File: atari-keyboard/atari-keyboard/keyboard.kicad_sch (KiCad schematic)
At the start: 210 parts, among them SW201 MENU, SW202 TURBO, SW203 RESET, SW204 OPTION, SW205 SELECT, SW206 START, SW207 HELP, SW208 ESC, SW209 RSHIFT, SW210 1, SW211 2, SW212 3, SW213 4, SW214 5, SW215 6, SW216 7, SW217 8, SW218 C_UP, SW219 9, SW220 0, SW221 LT, SW222 GT, SW223 BS, SW224 BRK, SW225 TAB, SW226 Q, SW227 C_DOWN, SW228 W, SW229 E, SW230 R, SW231 T, SW232 Y, SW233 U, SW234 I, SW235 O, SW236 C_LEFT, SW237 P, SW238 DASH, SW239 EQUAL, SW240 RET, SW241 CTRL, SW242 A, SW243 S, SW244 D, SW245 C_RIGHT, SW246 F, SW247 G, SW248 H, SW249 J, SW250 K, SW251 L, SW252 SEMI, SW253 PLUS, SW254 N, SW255 ASTRIX, SW256 CAPS, SW257 LSHIFT, SW258 Z, SW259 X, SW260 C, SW261 V, SW262 B, SW263 M, SW264 FN, SW265 INV, SW266 SPACE, SW267 COMMA, SW268 PERIOD, SW269 SLASH, SW270 POWER

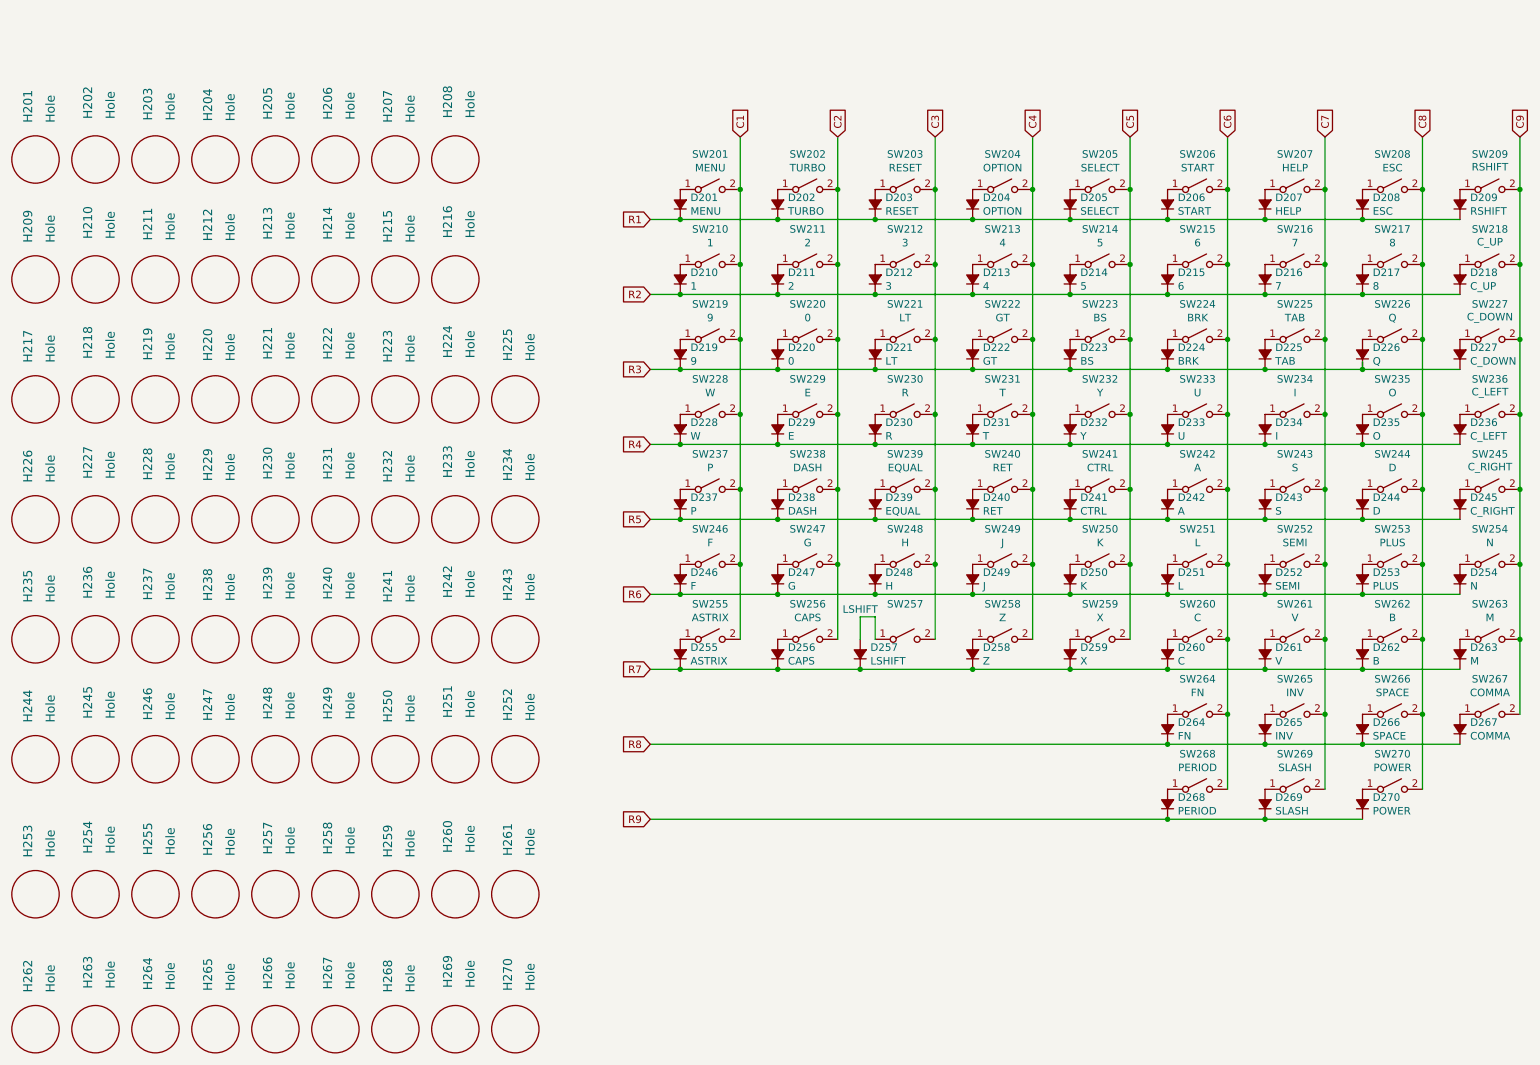
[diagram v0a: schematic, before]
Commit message: Reworked keyboard matrix to be a MUCH cleaner routing
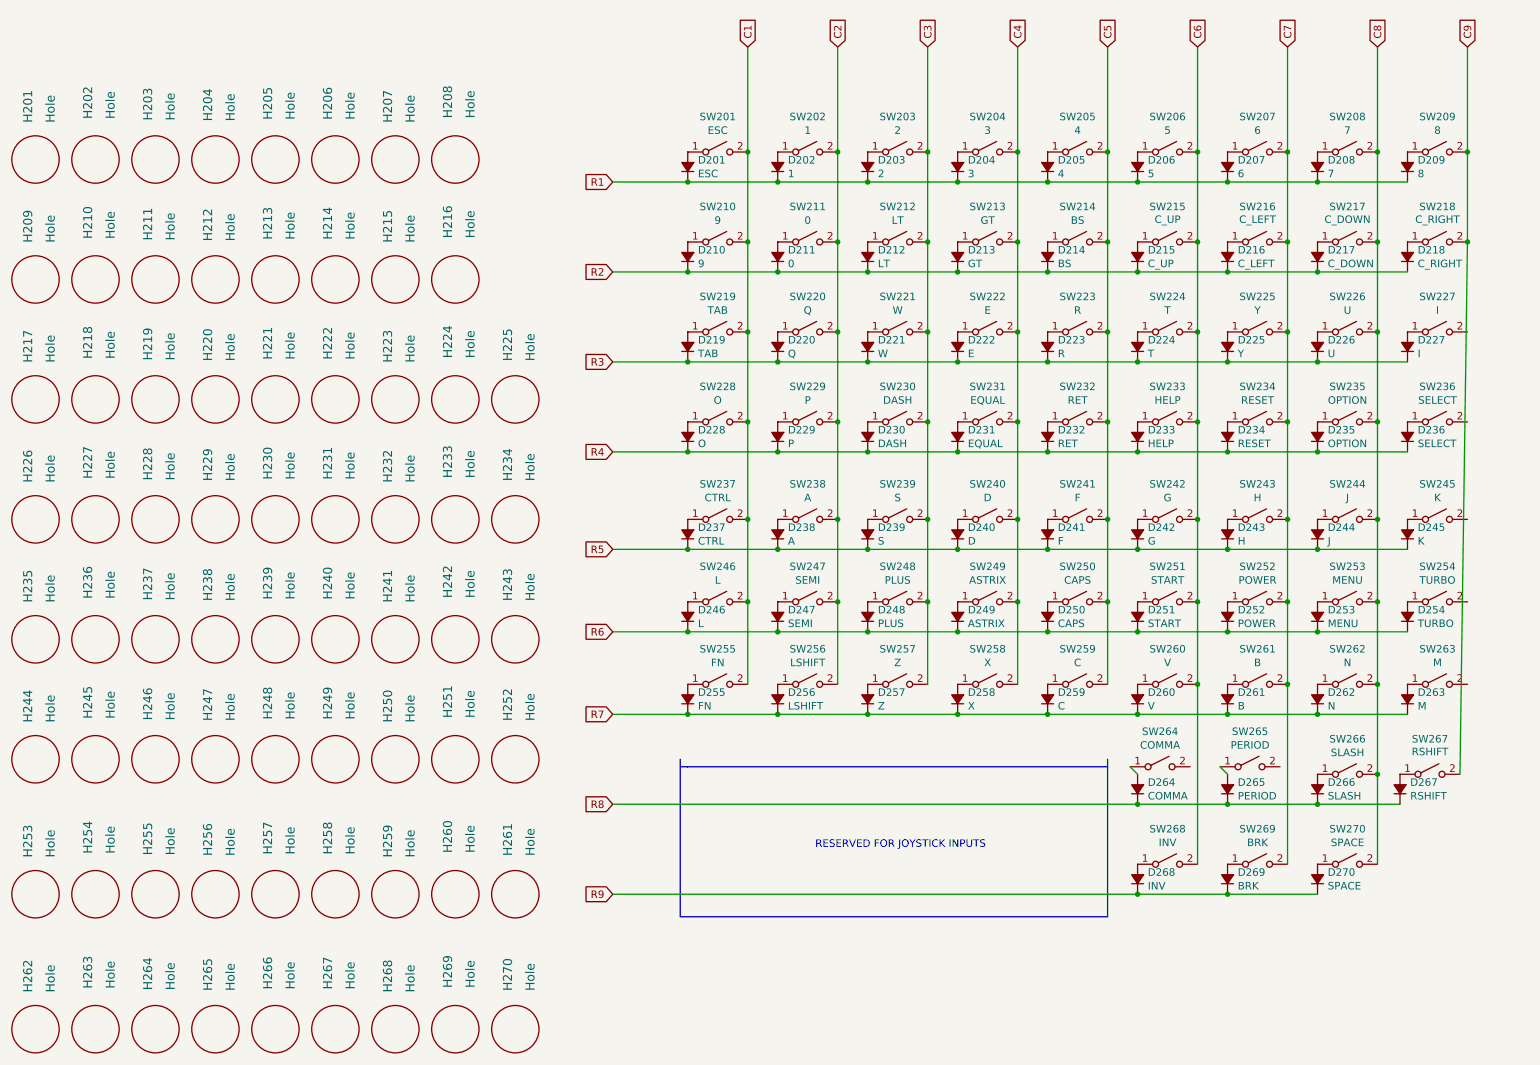
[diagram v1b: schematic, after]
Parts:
- removed D257: LSHIFT, retro-kbd:Diode-dual, symbol atari-keyboard-rescue:D_Small_ALT-Device
- removed SW257: LSHIFT, Button_Switch_Keyboard:SW_Cherry_MX_2.25u_PCB, symbol Switch:SW_SPST
- added D256: LSHIFT, retro-kbd:Diode-dual, symbol atari-keyboard-rescue:D_Small_ALT-Device
- added SW256: LSHIFT, Button_Switch_Keyboard:SW_Cherry_MX_2.00u_PCB, symbol Switch:SW_SPST
- H232: PCB_X (none) -> 4; PCB_Y (none) -> 7
- H240: PCB_X 4 -> (none); PCB_Y 7 -> (none)
- H256: PCB_Y (none) -> 5
- renumbered D208 to D201, D210 to D202, D211 to D203, D212 to D204, D213 to D205, D214 to D206, D215 to D207, D216 to D208, D217 to D209, D219 to D210, D220 to D211, D221 to D212, D222 to D213, D223 to D214, D218 to D215, D236 to D216, D227 to D217, D245 to D218, D225 to D219, D226 to D220, D228 to D221, D229 to D222, D230 to D223, D231 to D224, D232 to D225, D233 to D226, D234 to D227, D235 to D228, D237 to D229, D238 to D230, D239 to D231, D240 to D232, D207 to D233, D203 to D234, D204 to D235, D205 to D236, D241 to D237, D242 to D238, D243 to D239, D244 to D240, D246 to D241, D247 to D242, D248 to D243, D249 to D244, D250 to D245, D251 to D246, D252 to D247, D253 to D248, D255 to D249, D256 to D250, D206 to D251, D270 to D252, D201 to D253, D202 to D254, D264 to D255, D258 to D257, D259 to D258, D260 to D259, D261 to D260, D262 to D261, D254 to D262, D267 to D264, D268 to D265, D269 to D266, D209 to D267, D265 to D268, D224 to D269, D266 to D270, SW208 to SW201, SW210 to SW202, SW211 to SW203, SW212 to SW204, SW213 to SW205, SW214 to SW206, SW215 to SW207, SW216 to SW208, SW217 to SW209, SW219 to SW210, SW220 to SW211, SW221 to SW212, SW222 to SW213, SW223 to SW214, SW218 to SW215, SW236 to SW216, SW227 to SW217, SW245 to SW218, SW225 to SW219, SW226 to SW220, SW228 to SW221, SW229 to SW222, SW230 to SW223, SW231 to SW224, SW232 to SW225, SW233 to SW226, SW234 to SW227, SW235 to SW228, SW237 to SW229, SW238 to SW230, SW239 to SW231, SW240 to SW232, SW207 to SW233, SW203 to SW234, SW204 to SW235, SW205 to SW236, SW241 to SW237, SW242 to SW238, SW243 to SW239, SW244 to SW240, SW246 to SW241, SW247 to SW242, SW248 to SW243, SW249 to SW244, SW250 to SW245, SW251 to SW246, SW252 to SW247, SW253 to SW248, SW255 to SW249, SW256 to SW250, SW206 to SW251, SW270 to SW252, SW201 to SW253, SW202 to SW254, SW264 to SW255, SW258 to SW257, SW259 to SW258, SW260 to SW259, SW261 to SW260, SW262 to SW261, SW254 to SW262, SW267 to SW264, SW268 to SW265, SW269 to SW266, SW209 to SW267, SW265 to SW268, SW224 to SW269, SW266 to SW270
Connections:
- net C1: now also SW201.2 (B), SW219.2 (B), SW228.2 (B), SW237.2 (B), SW246.2 (B), SW255.2 (B); no longer SW202.2 (B), SW221.2 (B), SW229.2 (B), SW241.2 (B), SW249.2 (B), SW253.2 (B)
- net C2: now also SW202.2 (B), SW220.2 (B), SW229.2 (B), SW238.2 (B), SW247.2 (B), SW256.2 (B); no longer SW203.2 (B), SW222.2 (B), SW230.2 (B), SW242.2 (B), SW250.2 (B), SW254.2 (B)
- net C3: now also SW203.2 (B), SW221.2 (B), SW230.2 (B), SW239.2 (B), SW248.2 (B), SW257.2 (B); no longer SW204.2 (B), SW223.2 (B), SW231.2 (B), SW234.2 (B), SW243.2 (B)
- net C4: now also SW204.2 (B), SW222.2 (B), SW231.2 (B), SW240.2 (B), SW249.2 (B), SW258.2 (B); no longer SW205.2 (B), SW224.2 (B), SW232.2 (B), SW235.2 (B), SW244.2 (B), SW257.2 (B)
- net C5: now also SW205.2 (B), SW223.2 (B), SW232.2 (B), SW241.2 (B), SW250.2 (B), SW259.2 (B); no longer SW206.2 (B), SW225.2 (B), SW236.2 (B), SW237.2 (B), SW245.2 (B), SW258.2 (B)
- net C6: now also SW206.2 (B), SW215.2 (B), SW224.2 (B), SW233.2 (B), SW242.2 (B), SW260.2 (B), SW268.2 (B); no longer SW207.2 (B), SW226.2 (B), SW238.2 (B), SW246.2 (B), SW255.2 (B), SW259.2 (B), SW265.2 (B), SW269.2 (B)
- net C7: now also SW207.2 (B), SW216.2 (B), SW225.2 (B), SW234.2 (B), SW243.2 (B), SW252.2 (B), SW261.2 (B), SW269.2 (B); no longer SW208.2 (B), SW219.2 (B), SW227.2 (B), SW233.2 (B), SW239.2 (B), SW247.2 (B), SW260.2 (B), SW266.2 (B), SW268.2 (B)
- net C8: now also SW208.2 (B), SW217.2 (B), SW226.2 (B), SW235.2 (B), SW244.2 (B), SW253.2 (B), SW262.2 (B), SW266.2 (B); no longer SW201.2 (B), SW209.2 (B), SW220.2 (B), SW228.2 (B), SW240.2 (B), SW248.2 (B), SW252.2 (B), SW261.2 (B)
- net C9: now also SW209.2 (B); no longer SW215.2 (B), SW216.2 (B), SW217.2 (B), SW262.2 (B), SW263.2 (B), SW264.2 (B)
- net R1: now also D202.1 (K), D203.1 (K), D204.1 (K), D205.1 (K), D206.1 (K), D207.1 (K), D208.1 (K), D209.1 (K); no longer D233.1 (K), D234.1 (K), D235.1 (K), D236.1 (K), D251.1 (K), D253.1 (K), D254.1 (K), D267.1 (K)
- net R2: now also D210.1 (K), D211.1 (K), D212.1 (K), D213.1 (K), D214.1 (K), D216.1 (K), D217.1 (K), D218.1 (K); no longer D202.1 (K), D203.1 (K), D204.1 (K), D205.1 (K), D206.1 (K), D207.1 (K), D208.1 (K), D209.1 (K)
- net R3: now also D221.1 (K), D222.1 (K), D223.1 (K), D224.1 (K), D225.1 (K), D226.1 (K), D227.1 (K); no longer D210.1 (K), D211.1 (K), D212.1 (K), D213.1 (K), D214.1 (K), D217.1 (K), D269.1 (K)
- net R4: now also D229.1 (K), D230.1 (K), D231.1 (K), D232.1 (K), D233.1 (K), D234.1 (K), D235.1 (K), D236.1 (K); no longer D216.1 (K), D221.1 (K), D222.1 (K), D223.1 (K), D224.1 (K), D225.1 (K), D226.1 (K), D227.1 (K)
- net R5: now also D241.1 (K), D242.1 (K), D243.1 (K), D244.1 (K), D245.1 (K); no longer D218.1 (K), D229.1 (K), D230.1 (K), D231.1 (K), D232.1 (K)
- net R6: now also D249.1 (K), D250.1 (K), D251.1 (K), D252.1 (K), D253.1 (K), D254.1 (K); no longer D241.1 (K), D242.1 (K), D243.1 (K), D244.1 (K), D245.1 (K), D262.1 (K)
- net R7: now also D255.1 (K), D262.1 (K), D256.1 (K); no longer D249.1 (K), D250.1 (K)
- net R8: now also D265.1 (K), D266.1 (K), D267.1 (K); no longer D255.1 (K), D268.1 (K), D270.1 (K)
- net R9: now also D268.1 (K), D269.1 (K), D270.1 (K); no longer D252.1 (K), D265.1 (K), D266.1 (K)
- new net: D256.2 (A), SW256.1 (A)
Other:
- note added: "RESERVED FOR JOYSTICK INPUTS"
- moved on the sheet: D201, D202, D203, D204, D205, D206, D207, D208, D209, D210, D211, D212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

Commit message: Fixed the size of the LSHIFT
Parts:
- SW256: footprint Button_Switch_Keyboard:SW_Cherry_MX_2.00u_PCB -> Button_Switch_Keyboard:SW_Cherry_MX_2.25u_PCB
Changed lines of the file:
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@@
     (property "Reference" "SW256" (id 0) (at 158.75 121.031 0))
     (property "Value" "LSHIFT" (id 1) (at 158.75 123.3424 0))
-    (property "Footprint" "Button_Switch_Keyboard:SW_Cherry_MX_2.00u_PCB" (id 2) (at 158.75 127 0)
+    (property "Footprint" "Button_Switch_Keyboard:SW_Cherry_MX_2.25u_PCB" (id 2) (at 158.75 127 0)
       (effects (font (size 1.27 1.27)) hide)
     )

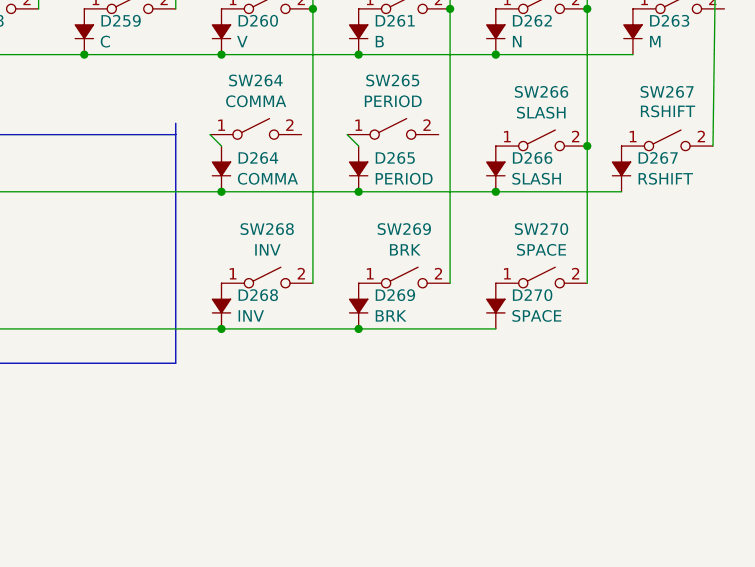
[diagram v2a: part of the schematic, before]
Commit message: Resolved a number of issues of keycaps not rendering correctly
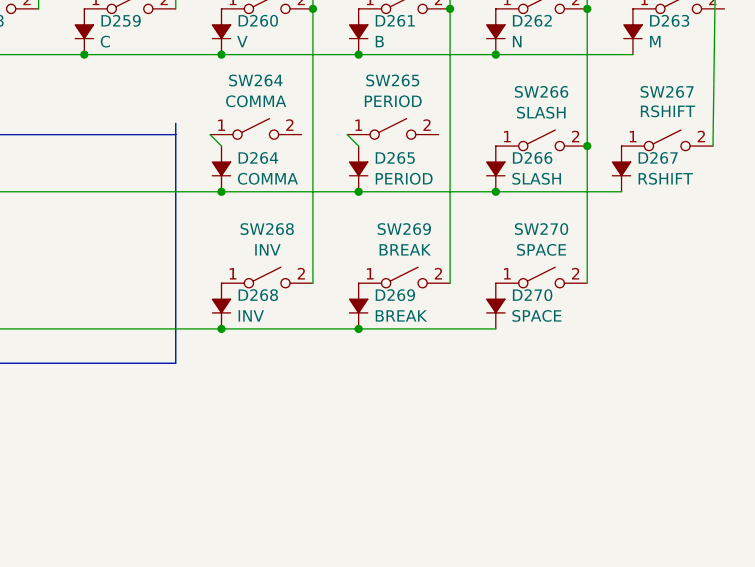
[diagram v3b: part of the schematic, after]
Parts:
- D269, SW269: value BRK -> BREAK
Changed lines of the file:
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@@
     (in_bom yes) (on_board yes)
     (property "Reference" "SW269" (id 0) (at 234.95 151.511 0))
-    (property "Value" "BRK" (id 1) (at 234.95 153.8224 0))
+    (property "Value" "BREAK" (id 1) (at 234.95 153.8224 0))
     (property "Footprint" "Button_Switch_Keyboard:SW_Cherry_MX_1.00u_PCB" (id 2) (at 234.95 157.48 0)
       (effects (font (size 1.27 1.27)) hide)
@@
       (effects (font (size 1.27 1.27)) (justify right))
     )
-    (property "Value" "BRK" (id 1) (at 231.5972 161.163 90)
-      (effects (font (size 1.27 1.27)) (justify right))
-    )
+    (property "Value" "BREAK" (id 1) (at 231.5972 161.163 90)
+      (effects (font (size 1.27 1.27)) (justify right))
+    )
